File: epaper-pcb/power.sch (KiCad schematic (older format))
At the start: 24 parts, among them J3 BATT, J3 USB_C_Receptacle_USB2.0, Q1 DMG3404L, Q2 AO3401A, SW1 SW_Push, U2 AMS1117-3.3, U3 LTC4054ES5-4.2

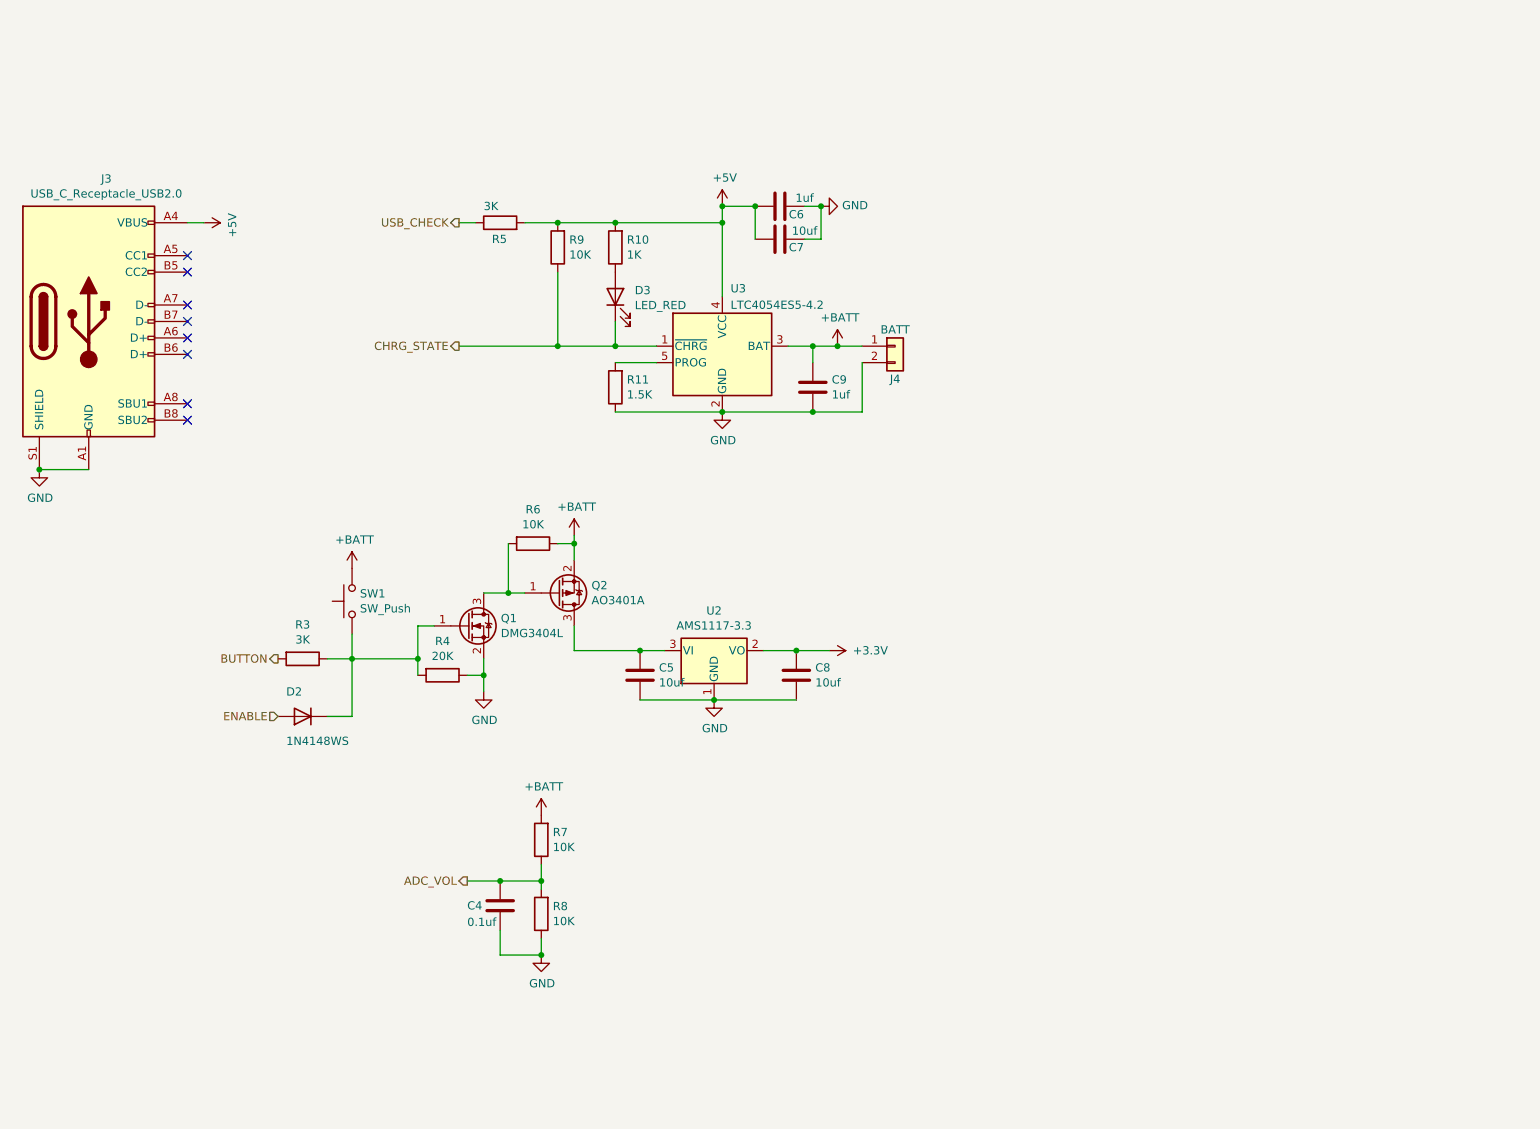
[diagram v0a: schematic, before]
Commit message: feat(pcb): add pcb design
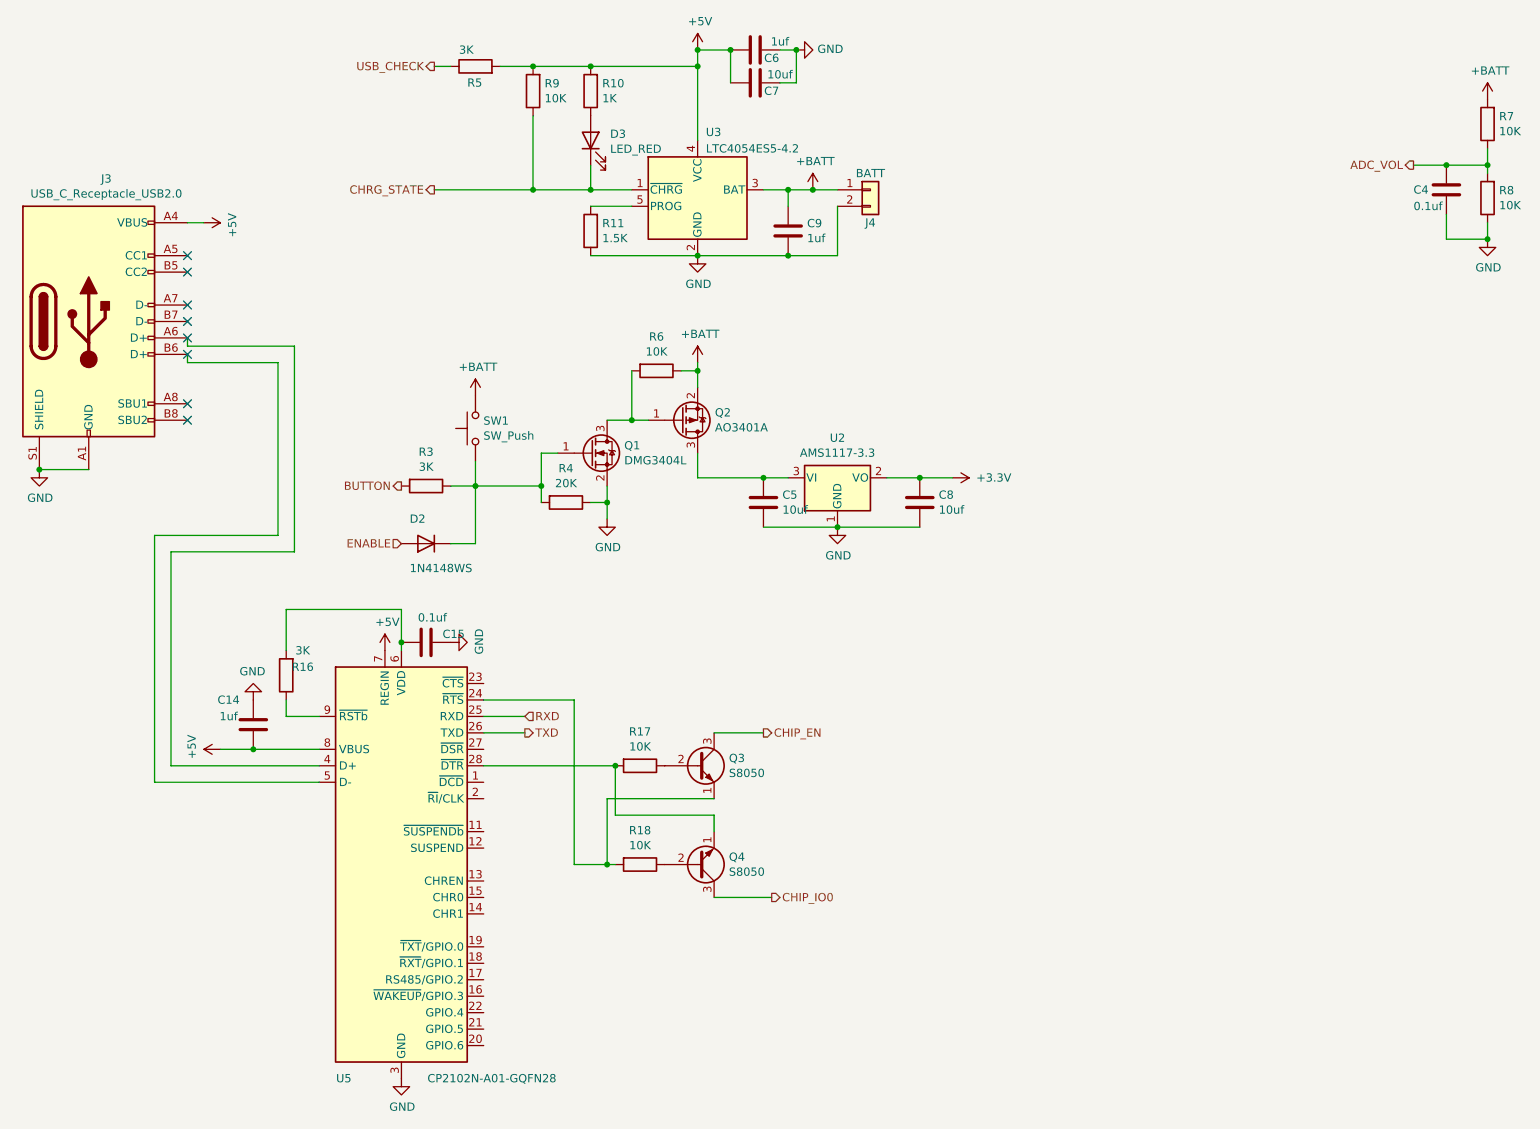
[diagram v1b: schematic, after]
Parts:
- added C14: 1uf, Capacitor_SMD:C_0603_1608Metric, symbol Device:C
- added C15: 0.1uf, Capacitor_SMD:C_0402_1005Metric, symbol Device:C
- added Q3, Q4: S8050, Package_TO_SOT_SMD:SOT-23, symbol Transistor_BJT:S8050
- added R16: 3K, Resistor_SMD:R_0402_1005Metric, symbol Device:R
- added R17, R18: 10K, Resistor_SMD:R_0402_1005Metric, symbol Device:R
- added U5: CP2102N-A01-GQFN28, Package_DFN_QFN:QFN-28-1EP_5x5mm_P0.5mm_EP3.35x3.35mm, symbol Interface_USB:CP2102N-A01-GQFN28
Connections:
- net +5V: now also C14.1, U5.7 (REGIN), U5.8 (VBUS)
- net GND: now also C14.2, C15.1, U5.29 (GND), U5.3 (GND)
- net at J3.A6 (D+): now also U5.4 (D+)
- net at J3.B6 (D+): now also U5.5 (D-)
- new net: Q3.1 (E), R18.2, U5.24 (~RTS)
- new net: Q4.1 (E), R17.2, U5.28 (~DTR)
- new net: C15.2, R16.2, U5.6 (VDD)
- new net: R16.1, U5.9 (~RSTb)
- new net: Q3.2 (B), R17.1
- new net: Q4.2 (B), R18.1
- new net CHIP_EN: Q3.3 (C)
- new net CHIP_IO0: Q4.3 (C)
- new net RXD: U5.25 (RXD)
- new net TXD: U5.26 (TXD)
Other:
- moved on the sheet: C4, C5, C6, C7, C8, C9, D2, D3, J4, Q1, Q2, R10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

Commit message: feat(pcb): add pcb line design
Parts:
- added R19, R20: 22, Resistor_SMD:R_0402_1005Metric, symbol Device:R
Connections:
- net at J3.A6 (D+): now also J3.B6 (D+), R20.2; no longer U5.4 (D+)
- net at J3.A7 (D-): now also J3.B7 (D-), R19.2
- net at U5.5 (D-): now also R19.1; no longer J3.B6 (D+)
- new net: R20.1, U5.4 (D+)
- no-connect marks 8 -> 20
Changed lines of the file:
@@
 NoConn ~ 2150 2250
 NoConn ~ 2150 2350
-NoConn ~ 2150 2550
-NoConn ~ 2150 2650
-NoConn ~ 2150 2750
-NoConn ~ 2150 2850
 NoConn ~ 2150 3150
 NoConn ~ 2150 3250
@@
 	2050 5350 2050 4050
 Wire Wire Line
-	2050 4050 2800 4050
-Wire Wire Line
-	2800 4050 2800 2800
-Wire Wire Line
-	2800 2800 2150 2800
-Wire Wire Line
-	2150 2800 2150 2750
-Wire Wire Line
 	2950 5450 1950 5450
 Wire Wire Line
 	1950 5450 1950 3950
 Wire Wire Line
-	1950 3950 2700 3950
-Wire Wire Line
-	2700 3950 2700 2900
-Wire Wire Line
-	2700 2900 2150 2900
-Wire Wire Line
-	2150 2900 2150 2850
+	2150 2750 2150 2850
+Wire Wire Line
+	2150 2650 2150 2550
+$Comp
+L Device:R R19
+U 1 1 5F524A26
+P 2550 3350
+F 0 "R19" H 2650 3400 50  0000 C CNN
+F 1 "22" H 2650 3300 50  0000 C CNN
+F 2 "Resistor_SMD:R_0402_1005Metric" V 2480 3350 50  0001 C CNN
+F 3 "~" H 2550 3350 50  0001 C CNN
+	1    2550 3350
+	-1   0    0    1
+$EndComp
+$Comp
+L Device:R R20
+U 1 1 5F525525
+P 2750 3350
+F 0 "R20" H 2850 3400 50  0000 C CNN
+F 1 "22" H 2850 3300 50  0000 C CNN
+F 2 "Resistor_SMD:R_0402_1005Metric" V 2680 3350 50  0001 C CNN
+F 3 "~" H 2750 3350 50  0001 C CNN
+	1    2750 3350
+	-1   0    0    1
+$EndComp
+Wire Wire Line
+	2150 2550 2550 2550
+Wire Wire Line
+	2550 2550 2550 3200
+Connection ~ 2150 2550
+Wire Wire Line
+	2150 2750 2750 2750
+Wire Wire Line
+	2750 2750 2750 3200
+Connection ~ 2150 2750
+Wire Wire Line
+	1950 3950 2550 3950
+Wire Wire Line
+	2550 3950 2550 3500
+Wire Wire Line
+	2050 4050 2750 4050
+Wire Wire Line
+	2750 4050 2750 3500
+NoConn ~ 3950 4850
+NoConn ~ 3950 5250
+NoConn ~ 3950 5450
+NoConn ~ 3950 5550
+NoConn ~ 3950 5750
+NoConn ~ 3950 5850
+NoConn ~ 3950 6250
+NoConn ~ 3950 6150
+NoConn ~ 3950 6050
+NoConn ~ 3950 6450
+NoConn ~ 3950 6550
+NoConn ~ 3950 6650
+NoConn ~ 3950 6750
+NoConn ~ 3950 6850
+NoConn ~ 3950 6950
+NoConn ~ 3950 7050
 $EndSCHEMATC

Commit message: feat(pcb): compeleted pcb line design
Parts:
- added D4: 1N4148WS, Diode_SMD:D_SOD-323, symbol Diode:1N4148WS
- R16: value 3K -> 10K
- R3, R5: value 3K -> 4.7K
- R4: value 20K -> 10K
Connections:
- net at D2.1 (K), Q1.1 (G), R4.2: now also D4.1 (K); no longer R3.1, SW1.1
- new net: D4.2 (A), R3.1, SW1.1
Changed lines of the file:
@@
 AR Path="/5F4ECFED/5F5408A3" Ref="R5"  Part="1"
 F 0 "R5" V 3800 1150 50  0000 R CNN
-F 1 "3K" V 4000 1200 50  0000 R CNN
+F 1 "4.7K" V 4000 1200 50  0000 R CNN
 F 2 "Resistor_SMD:R_0402_1005Metric" V 3830 1100 50  0001 C CNN
 F 3 "~" H 3900 1100 50  0001 C CNN
@@
 P 4450 3750
 F 0 "R4" V 4243 3750 50  0000 C CNN
-F 1 "20K" V 4334 3750 50  0000 C CNN
+F 1 "10K" V 4334 3750 50  0000 C CNN
 F 2 "Resistor_SMD:R_0402_1005Metric" V 4380 3750 50  0001 C CNN
 F 3 "~" H 4450 3750 50  0001 C CNN
@@
 Wire Wire Line
 	4400 3450 4300 3450
-Wire Wire Line
-	4300 3450 4300 3650
 $Comp
 L power:+BATT #PWR0121
@@
 $EndComp
 Wire Wire Line
-	3900 3650 4300 3650
-Connection ~ 4300 3650
-Wire Wire Line
-	4300 3650 4300 3750
-Wire Wire Line
 	3900 3500 3900 3650
 Wire Wire Line
 	3750 3650 3900 3650
-Connection ~ 3900 3650
 $Comp
 L Device:R R3
@@
 P 3600 3650
 F 0 "R3" V 3393 3650 50  0000 C CNN
-F 1 "3K" V 3484 3650 50  0000 C CNN
+F 1 "4.7K" V 3484 3650 50  0000 C CNN
 F 2 "Resistor_SMD:R_0402_1005Metric" V 3530 3650 50  0001 C CNN
 F 3 "~" H 3600 3650 50  0001 C CNN
@@
 	0    1    1    0
 $EndComp
-Wire Wire Line
-	3900 4000 3900 3650
-Wire Wire Line
-	3750 4000 3900 4000
 Text HLabel 3450 4000 0    50   Input ~ 0
 ENABLE
@@
 P 2750 4800
 F 0 "R16" H 2650 4750 50  0000 C CNN
-F 1 "3K" H 2650 4650 50  0000 C CNN
+F 1 "10K" H 2650 4650 50  0000 C CNN
 F 2 "Resistor_SMD:R_0402_1005Metric" V 2680 4800 50  0001 C CNN
 F 3 "~" H 2750 4800 50  0001 C CNN
@@
 NoConn ~ 3950 6950
 NoConn ~ 3950 7050
+$Comp
+L Diode:1N4148WS D4
+U 1 1 5F53E1F2
+P 4050 3650
+F 0 "D4" H 4150 3500 50  0000 R CNN
+F 1 "1N4148WS" H 4350 3800 50  0000 R CNN
+F 2 "Diode_SMD:D_SOD-323" H 4050 3475 50  0001 C CNN
+F 3 "https://www.vishay.com/docs/85751/1n4148ws.pdf" H 4050 3650 50  0001 C CNN
+	1    4050 3650
+	-1   0    0    1
+$EndComp
+Wire Wire Line
+	4300 3450 4300 3650
+Connection ~ 3900 3650
+Wire Wire Line
+	4200 4000 4200 3650
+Wire Wire Line
+	3750 4000 4200 4000
+Wire Wire Line
+	4200 3650 4300 3650
+Connection ~ 4200 3650
+Connection ~ 4300 3650
+Wire Wire Line
+	4300 3650 4300 3750
 $EndSCHEMATC
